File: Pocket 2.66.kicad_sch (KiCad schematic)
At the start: 85 parts, among them P1 USB-TYPE-C-018, P3 FPC-05F-24PH20, P4 HX-1.25-2AWB, Q1 HL2300, Q2 HL2305, SW1 TS-24CA-S16, SW2 TS-24CA-S16, SW3 TS-24CA-S16, U1 ESP32-C3FH4, U2 LCK-TF-027H30008-WLG, U3 GX4054, U4 GS2019-33TR5, U5 STC3115AIQT, U6 ESD-USB, X1 40MHz 9pF 2016

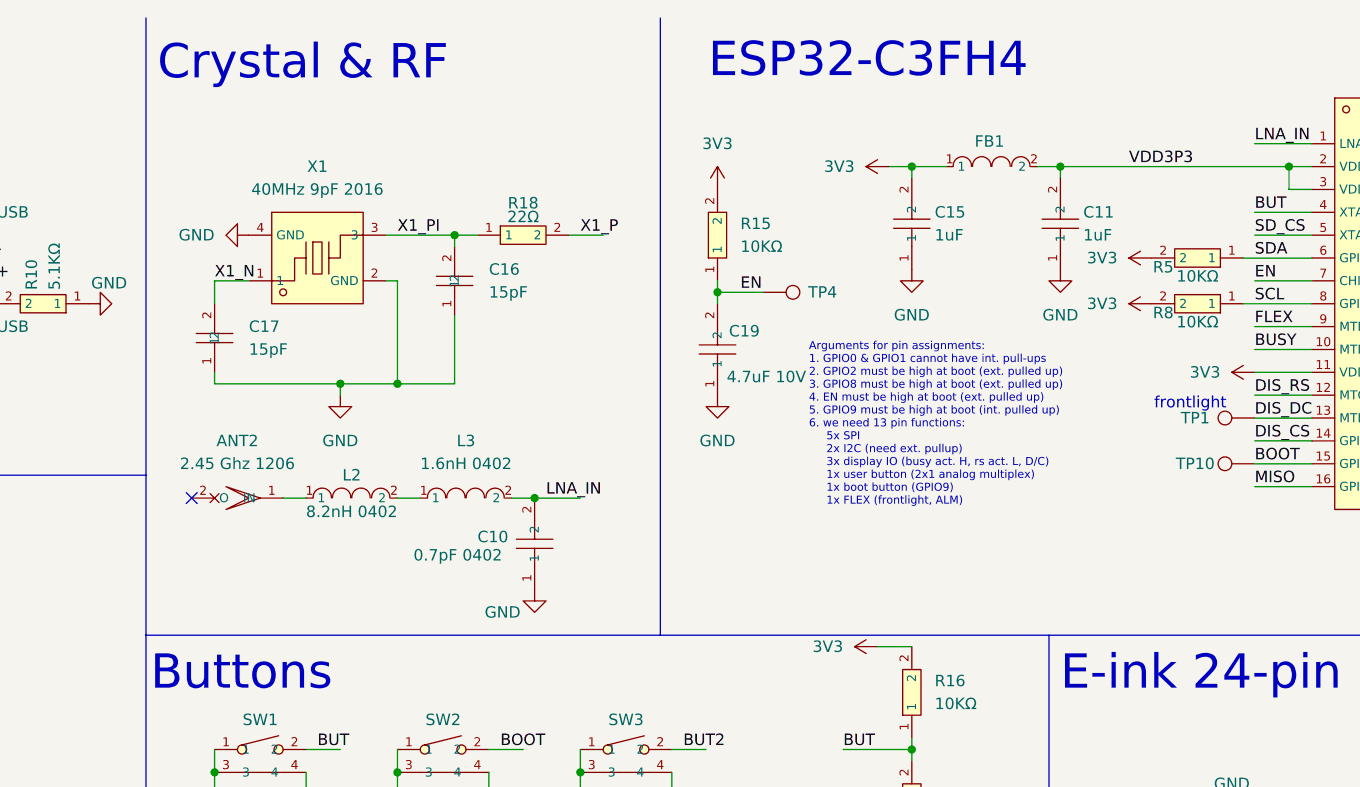
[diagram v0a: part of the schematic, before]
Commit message: Update RF on schematic and BOM details
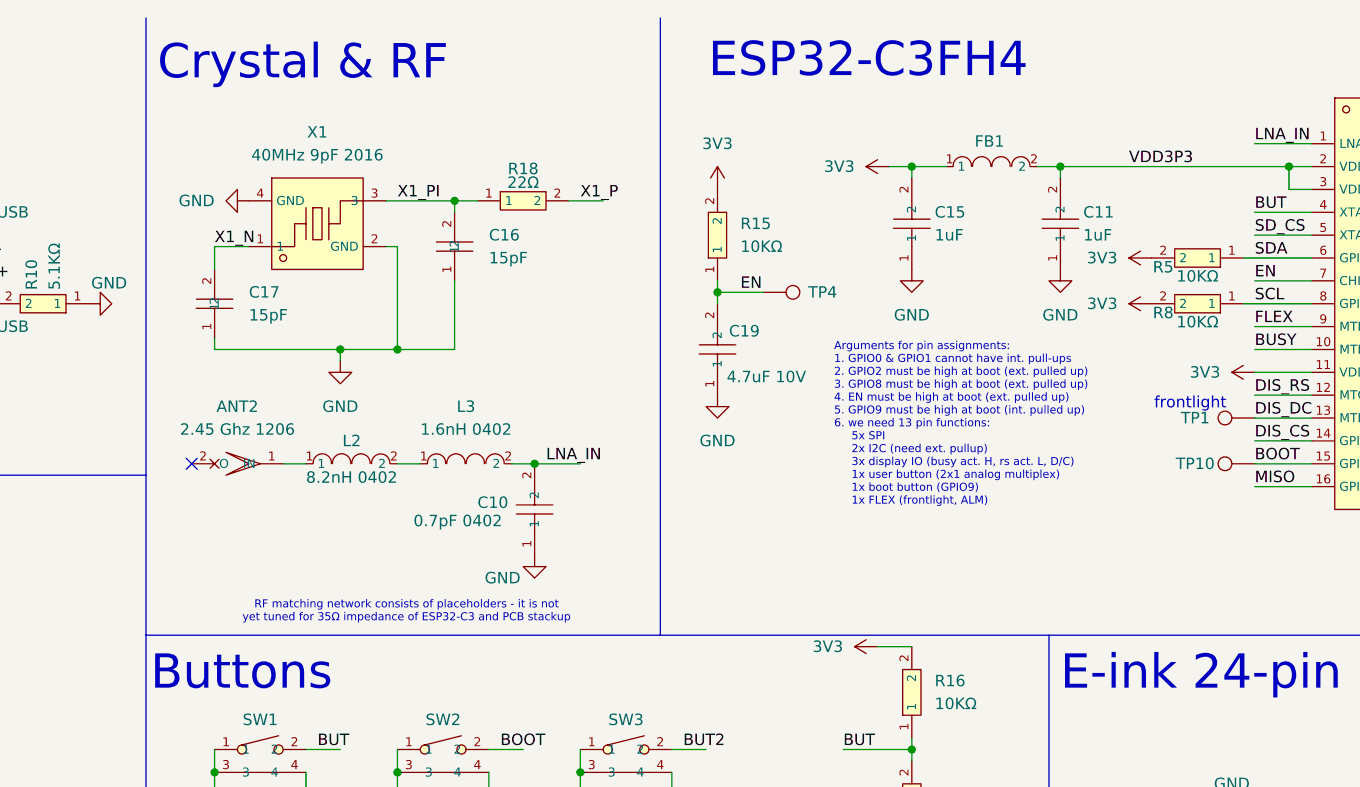
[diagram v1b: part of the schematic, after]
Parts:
- ANT2: JLC Type (none) -> Extended
- SH2: MPN (none) -> RL0603FR-070R025L
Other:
- note added: "RF matching network consists of placeholders - it is not yet tuned for 35Ω impedance of ESP32-C3 and PCB stackup"
- moved on the sheet: ANT2, C10, C16, C17, L2, L3, R18, X1

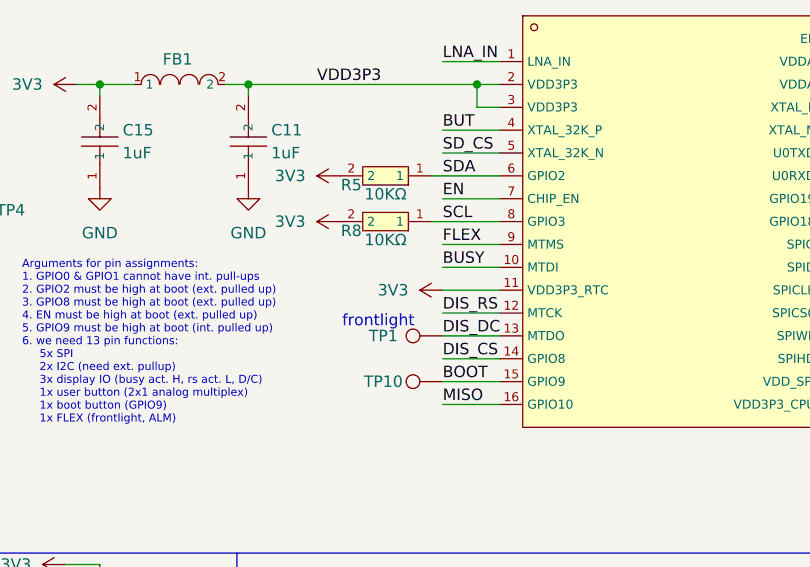
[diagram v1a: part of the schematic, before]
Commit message: Move 2R2 basic part to top side
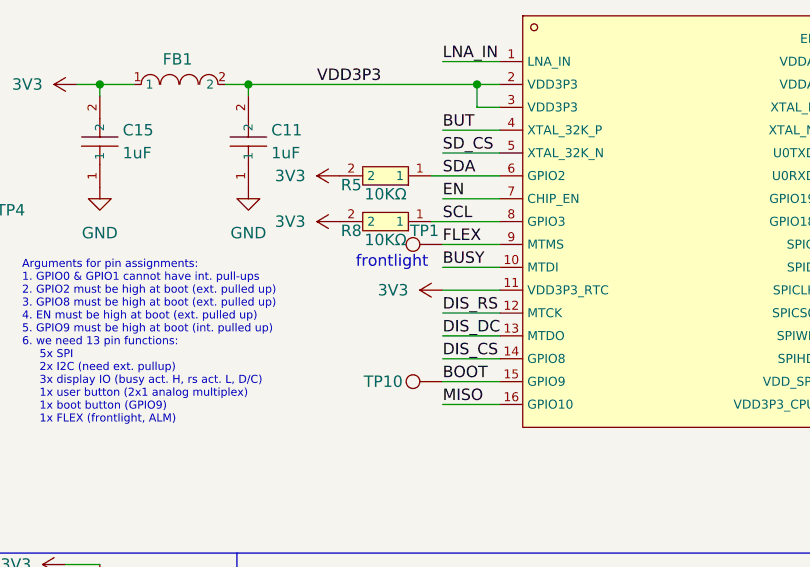
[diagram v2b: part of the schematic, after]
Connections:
- net DIS_DC: no longer TP1.1
- net FLEX: now also TP1.1
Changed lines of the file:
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@@
 	(text "frontlight\n"
 		(exclude_from_sim no)
-		(at 198.374 54.356 0)
+		(at 199.898 47.752 0)
 		(effects
 			(font
@@
 	)
 	(symbol
+		(lib_id "Connector:TestPoint")
+		(at 209.55 45.72 90)
+		(unit 1)
+		(body_style 1)
+		(exclude_from_sim no)
+		(in_bom no)
+		(on_board yes)
+		(in_pos_files yes)
+		(dnp no)
+		(property "Reference" "TP1"
+			(at 207.518 44.196 90)
+			(show_name no)
+			(do_not_autoplace no)
+			(effects
+				(font
+					(size 1.27 1.27)
+				)
+			)
+		)
+		(property "Value" "TestPoint"
+			(at 206.248 43.18 90)
+			(hide yes)
+			(show_name no)
+			(do_not_autoplace no)
+			(effects
+				(font
+					(size 1.27 1.27)
+				)
+			)
+		)
+		(property "Footprint" "TestPoint:TestPoint_Pad_D1.5mm"
+			(at 209.55 40.64 0)
+			(hide yes)
+			(show_name no)
+			(do_not_autoplace no)
+			(effects
+				(font
+					(size 1.27 1.27)
+				)
+			)
+		)
+		(property "Datasheet" ""
+			(at 209.55 40.64 0)
+			(hide yes)
+			(show_name no)
+			(do_not_autoplace no)
+			(effects
+				(font
+					(size 1.27 1.27)
+				)
+			)
+		)
+		(property "Description" "test point"
+			(at 209.55 45.72 0)
+			(hide yes)
+			(show_name no)
+			(do_not_autoplace no)
+			(effects
+				(font
+					(size 1.27 1.27)
+				)
+			)
+		)
+		(property "LCSC Type" ""
+			(at 209.55 45.72 90)
+			(hide yes)
+			(show_name no)
+			(do_not_autoplace no)
+			(effects
+				(font
+					(size 1.27 1.27)
+				)
+			)
+		)
+		(pin "1"
+		)
+		(instances
+			(project "Pocket 2.66"
+				(path "/1cd4c3f1-5659-46dd-b7c5-63c53cd89f06"
+					(reference "TP1")
+					(unit 1)
+				)
+			)
+		)
+	)
+	(symbol
 		(lib_id "power:GND")
 		(at 63.5 187.96 0)
@@
 					(unit 1)
 				)
-			)
-		)
-	)
-	(symbol
-		(lib_id "Connector:TestPoint")
-		(at 209.55 55.88 90)
-		(unit 1)
-		(body_style 1)
-		(exclude_from_sim no)
-		(in_bom no)
-		(on_board yes)
-		(in_pos_files yes)
-		(dnp no)
-		(property "Reference" "TP1"
-			(at 202.946 55.88 90)
-			(show_name no)
-			(do_not_autoplace no)
-			(effects
-				(font
-					(size 1.27 1.27)
-				)
-			)
-		)
-		(property "Value" "TestPoint"
-			(at 206.248 53.34 90)
-			(hide yes)
-			(show_name no)
-			(do_not_autoplace no)
-			(effects
-				(font
-					(size 1.27 1.27)
-				)
-			)
-		)
-		(property "Footprint" "TestPoint:TestPoint_Pad_D1.5mm"
-			(at 209.55 50.8 0)
-			(hide yes)
-			(show_name no)
-			(do_not_autoplace no)
-			(effects
-				(font
-					(size 1.27 1.27)
-				)
-			)
-		)
-		(property "Datasheet" ""
-			(at 209.55 50.8 0)
-			(hide yes)
-			(show_name no)
-			(do_not_autoplace no)
-			(effects
-				(font
-					(size 1.27 1.27)
-				)
-			)
-		)
-		(property "Description" "test point"
-			(at 209.55 55.88 0)
-			(hide yes)
-			(show_name no)
-			(do_not_autoplace no)
-			(effects
-				(font
-					(size 1.27 1.27)
-				)
-			)
-		)
-		(property "LCSC Type" ""
-			(at 209.55 55.88 90)
-			(hide yes)
-			(show_name no)
-			(do_not_autoplace no)
-			(effects
-				(font
-					(size 1.27 1.27)
-				)
-			)
-		)
-		(pin "1"
-		)
-		(instances
-			(project "Pocket 2.66"
-				(path "/1cd4c3f1-5659-46dd-b7c5-63c53cd89f06"
-					(reference "TP1")
-					(unit 1)
-				)

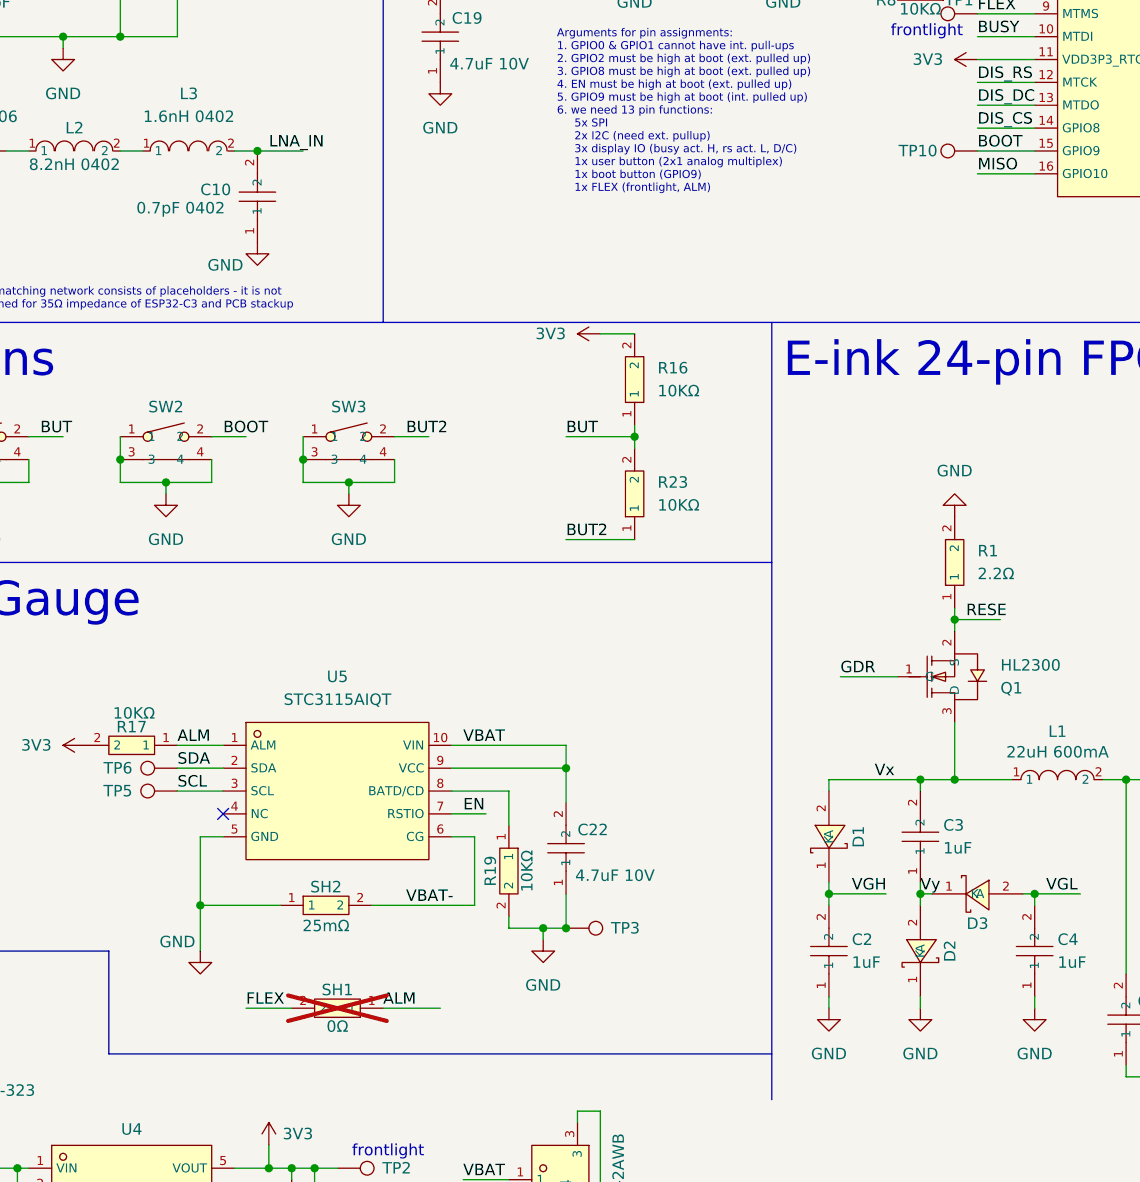
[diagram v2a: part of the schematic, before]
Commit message: Add extra test pads
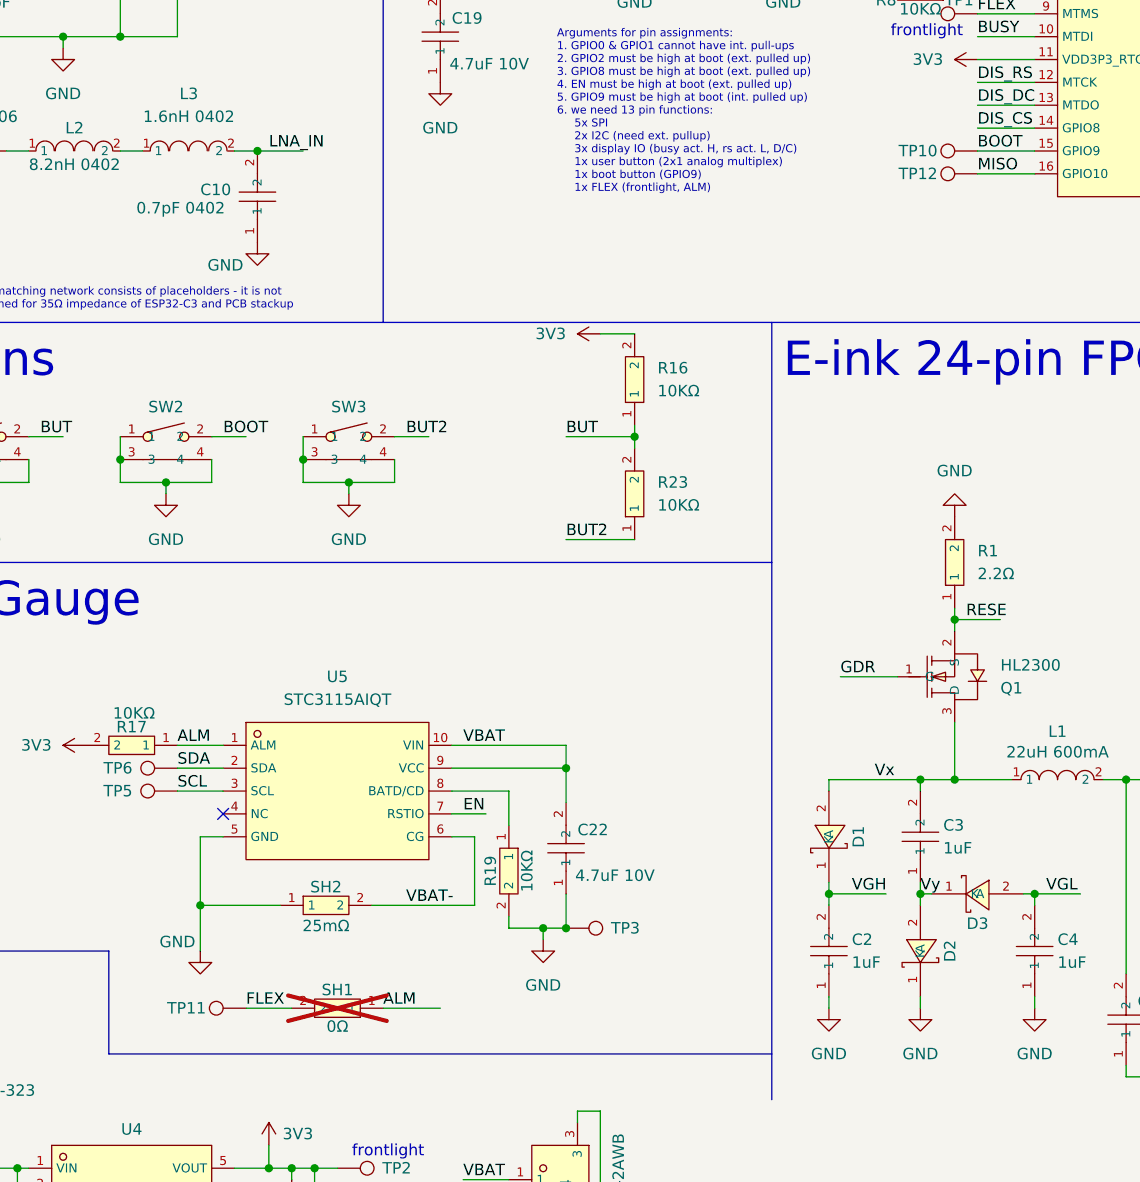
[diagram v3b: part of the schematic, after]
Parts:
- added TP11, TP12: TestPoint, TestPoint:TestPoint_Pad_D1.0mm, symbol Connector:TestPoint
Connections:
- net FLEX: now also TP11.1
- net MISO: now also TP12.1
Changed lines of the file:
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@@
 	)
 	(symbol
+		(lib_id "Connector:TestPoint")
+		(at 128.27 156.21 90)
+		(unit 1)
+		(body_style 1)
+		(exclude_from_sim no)
+		(in_bom no)
+		(on_board yes)
+		(in_pos_files yes)
+		(dnp no)
+		(property "Reference" "TP11"
+			(at 121.666 156.21 90)
+			(show_name no)
+			(do_not_autoplace no)
+			(effects
+				(font
+					(size 1.27 1.27)
+				)
+			)
+		)
+		(property "Value" "TestPoint"
+			(at 124.968 153.67 90)
+			(hide yes)
+			(show_name no)
+			(do_not_autoplace no)
+			(effects
+				(font
+					(size 1.27 1.27)
+				)
+			)
+		)
+		(property "Footprint" "TestPoint:TestPoint_Pad_D1.0mm"
+			(at 128.27 151.13 0)
+			(hide yes)
+			(show_name no)
+			(do_not_autoplace no)
+			(effects
+				(font
+					(size 1.27 1.27)
+				)
+			)
+		)
+		(property "Datasheet" ""
+			(at 128.27 151.13 0)
+			(hide yes)
+			(show_name no)
+			(do_not_autoplace no)
+			(effects
+				(font
+					(size 1.27 1.27)
+				)
+			)
+		)
+		(property "Description" "test point"
+			(at 128.27 156.21 0)
+			(hide yes)
+			(show_name no)
+			(do_not_autoplace no)
+			(effects
+				(font
+					(size 1.27 1.27)
+				)
+			)
+		)
+		(property "LCSC Type" ""
+			(at 128.27 156.21 90)
+			(hide yes)
+			(show_name no)
+			(do_not_autoplace no)
+			(effects
+				(font
+					(size 1.27 1.27)
+				)
+			)
+		)
+		(pin "1"
+		)
+		(instances
+			(project "Pocket 2.66"
+				(path "/1cd4c3f1-5659-46dd-b7c5-63c53cd89f06"
+					(reference "TP11")
+					(unit 1)
+				)
+			)
+		)
+	)
+	(symbol
 		(lib_id "LCSC Global:HL2300_C7420343")
 		(at 204.47 119.38 0)
@@
 					(unit 1)
 				)
+			)
+		)
+	)
+	(symbol
+		(lib_id "Connector:TestPoint")
+		(at 209.55 63.5 90)
+		(unit 1)
+		(body_style 1)
+		(exclude_from_sim no)
+		(in_bom no)
+		(on_board yes)
+		(in_pos_files yes)
+		(dnp no)
+		(property "Reference" "TP12"
+			(at 202.946 63.5 90)
+			(show_name no)
+			(do_not_autoplace no)
+			(effects
+				(font
+					(size 1.27 1.27)
+				)
+			)
+		)
+		(property "Value" "TestPoint"
+			(at 206.248 60.96 90)
+			(hide yes)
+			(show_name no)
+			(do_not_autoplace no)
+			(effects
+				(font
+					(size 1.27 1.27)
+				)
+			)
+		)
+		(property "Footprint" "TestPoint:TestPoint_Pad_D1.0mm"
+			(at 209.55 58.42 0)
+			(hide yes)
+			(show_name no)
+			(do_not_autoplace no)
+			(effects
+				(font
+					(size 1.27 1.27)
+				)
+			)
+		)
+		(property "Datasheet" ""
+			(at 209.55 58.42 0)
+			(hide yes)
+			(show_name no)
+			(do_not_autoplace no)
+			(effects
+				(font
+					(size 1.27 1.27)
+				)
+			)
+		)
+		(property "Description" "test point"
+			(at 209.55 63.5 0)
+			(hide yes)
+			(show_name no)
+			(do_not_autoplace no)
+			(effects
+				(font
+					(size 1.27 1.27)
+				)
+			)
+		)
+		(property "LCSC Type" ""
+			(at 209.55 63.5 90)
+			(hide yes)
+			(show_name no)
+			(do_not_autoplace no)
+			(effects
+				(font
+					(size 1.27 1.27)
+				)
+			)
+		)
+		(pin "1"
+		)
+		(instances
+			(project "Pocket 2.66"
+				(path "/1cd4c3f1-5659-46dd-b7c5-63c53cd89f06"
+					(reference "TP12")
+					(unit 1)
+				)
